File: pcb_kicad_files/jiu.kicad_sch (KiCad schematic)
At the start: 175 parts, among them J1 2x3 2.54mm pitch pin header, J2 TYPE-C-31-M-12, J3 1x5 2.54mm pitch pin header, J4 2x9 2.54mm pitch pin header, J5 Conn_01x02, Q1 2N7002, SW1 1U, SW10 1U, SW11 1U, SW12 1U, SW13 1U, SW14 1U, SW15 1U, SW16 2u, SW17 1.5U, SW18 1U, SW19 1U, SW2 1U, SW20 1U, SW21 1U, SW22 1U, SW23 1U, SW24 1U, SW25 1U, SW26 1U, SW27 1U, SW28 1U, SW29 1U, SW3 1U, SW30 1.5U, SW31 1U, SW32 1.75U, SW33 1U, SW34 1U, SW35 1U, SW36 1U, SW37 1U, SW38 1U, SW39 1U, SW4 1U, SW40 1U, SW41 1U, SW42 1U, SW43 1U, SW44 2.25U, SW45 1U, SW46 1.25U, SW47 2.25U, SW48 1U, SW49 1U, SW5 1U, SW50 1U, SW51 1U, SW52 1U, SW53 1U, SW54 1U, SW55 1U, SW56 1U, SW57 1U, SW58 1.75U, SW59 1U, SW6 1U, SW60 1U, SW61 1.5U, SW62 1U, SW63 1.5U, SW64 7U, SW65 1.5U, SW66 1U, SW67 1U, SW68 1U, SW69 1.25U, SW7 1U, SW70 1.25U, SW71 1.25U, SW72 6.25U, SW73 1.25U, SW8 1U, SW9 1U, U1 SRV05-4-P-T7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

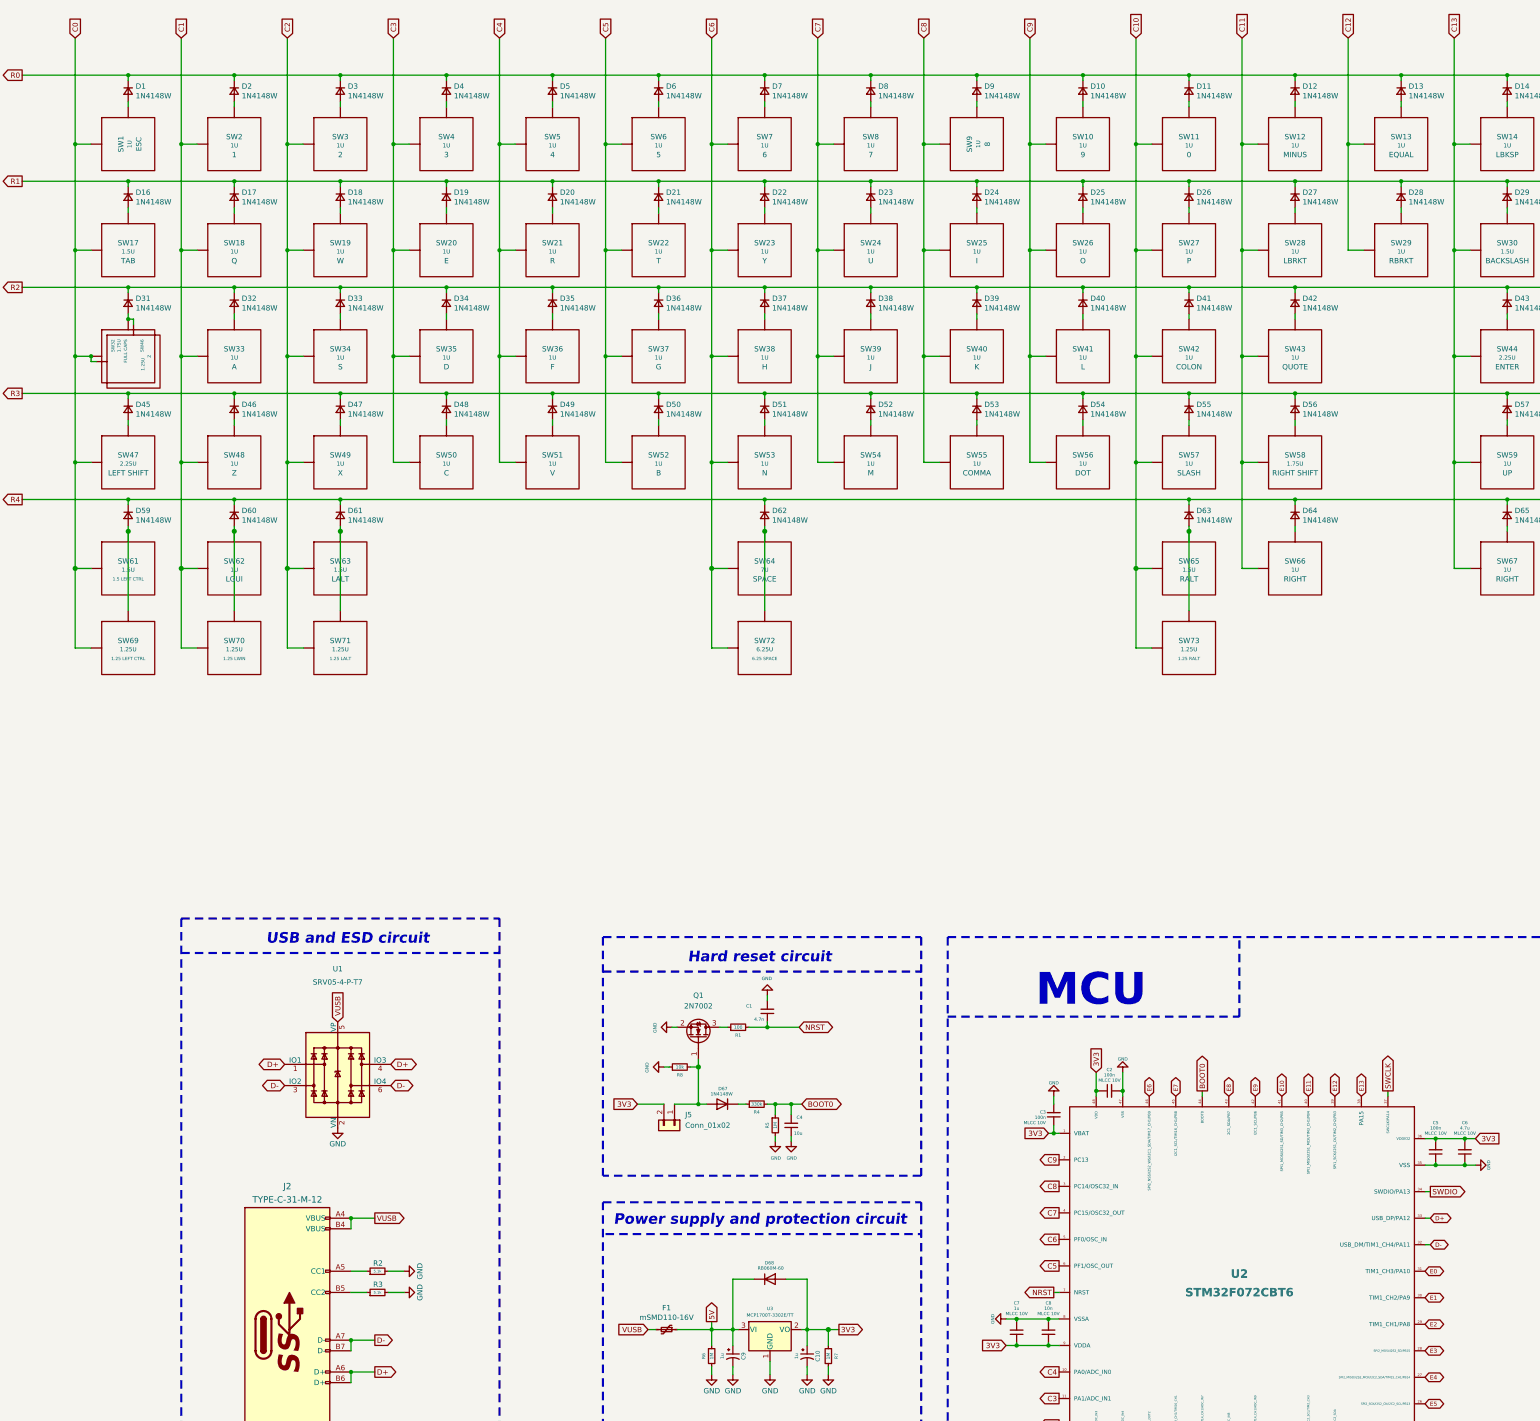
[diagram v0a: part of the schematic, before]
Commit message: Remove pin header connectors from BoM
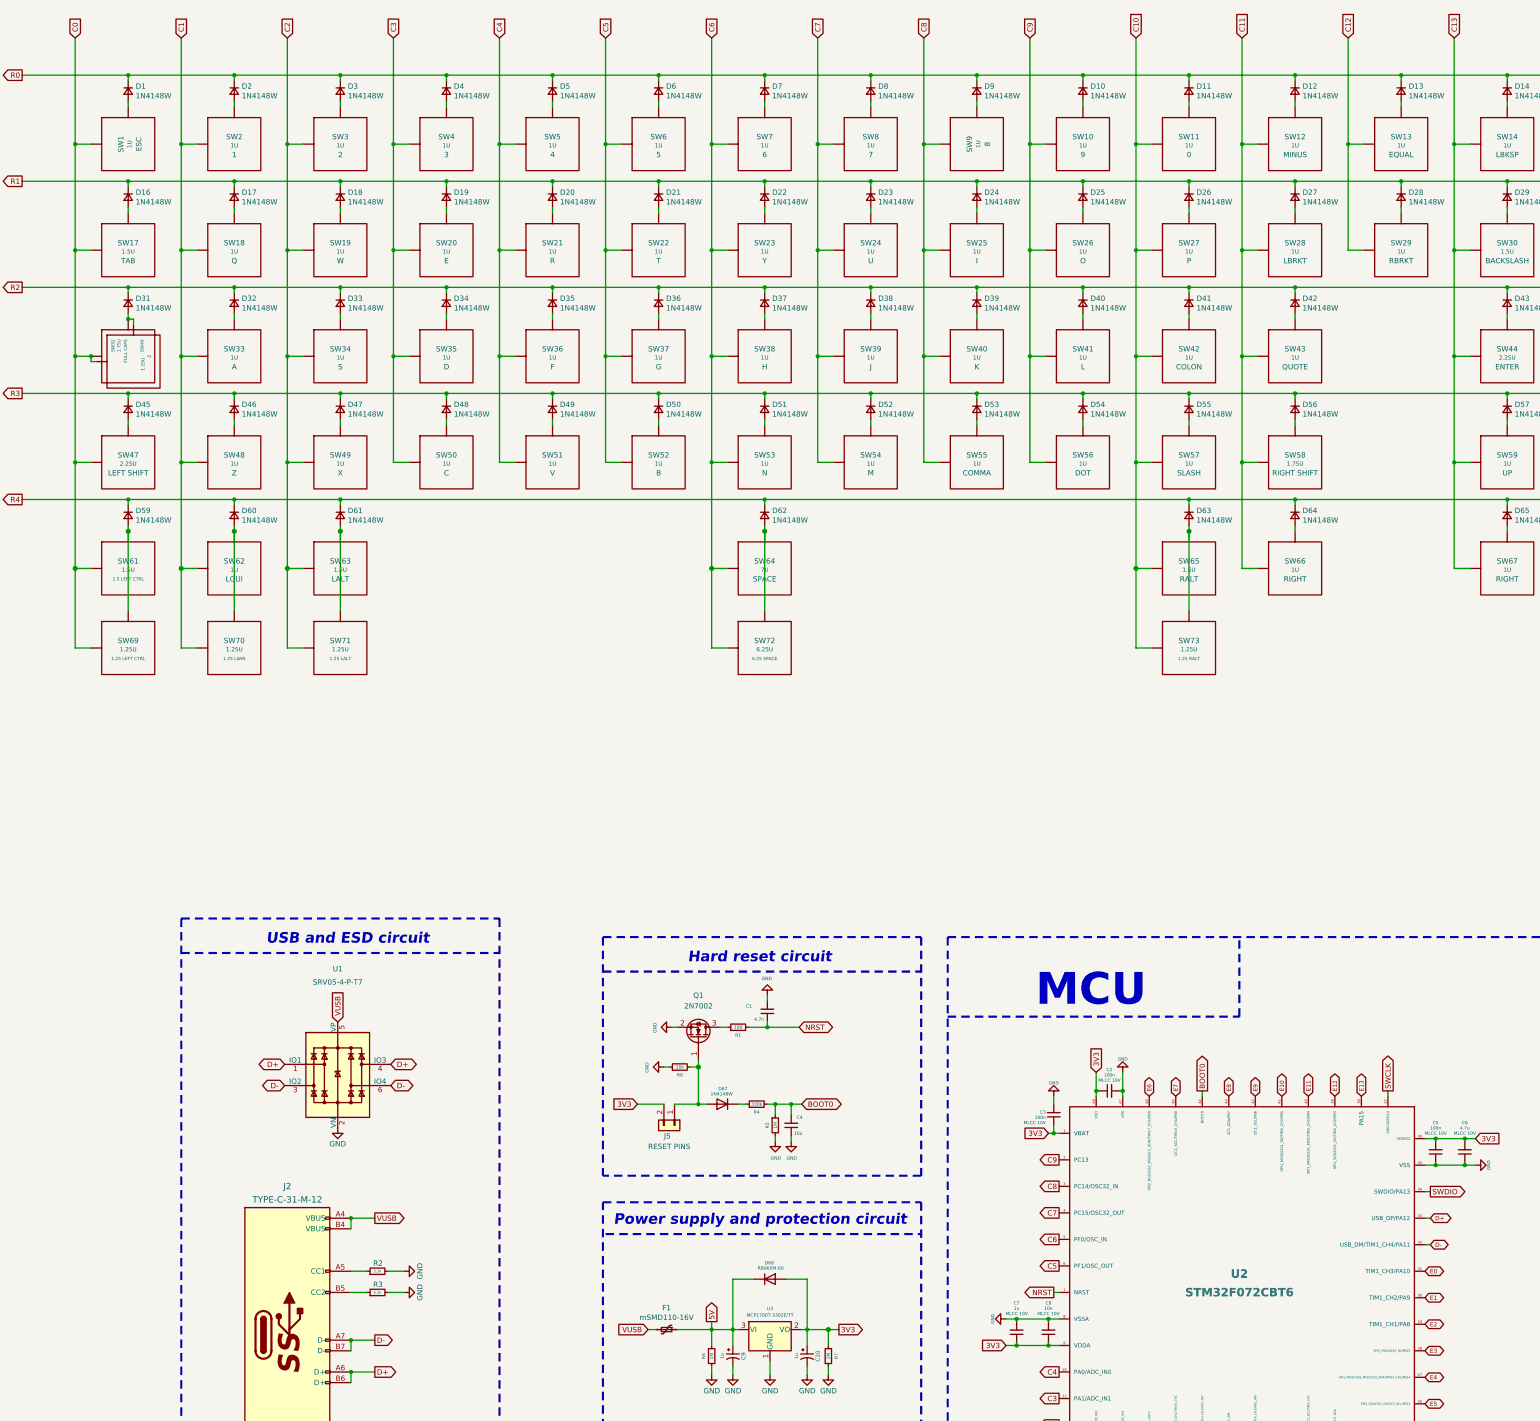
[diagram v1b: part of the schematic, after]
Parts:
- J3, J4: now left out of the parts list
- J5: value Conn_01x02 -> RESET PINS; Specification (none) -> Two THT pins for MCU hardware reset; now left out of the parts list
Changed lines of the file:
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@@
     (stroke (width 0) (type solid) (color 0 0 0 0))
   )
-  (wire (pts (xy 38.1 50.8) (xy 38.1 76.2))
+  (wire (pts (xy 38.1 50.8) (xy 41.91 50.8))
     (stroke (width 0) (type solid) (color 0 0 0 0))
   )
-  (wire (pts (xy 38.1 50.8) (xy 41.91 50.8))
+  (wire (pts (xy 38.1 76.2) (xy 38.1 50.8))
     (stroke (width 0) (type solid) (color 0 0 0 0))
   )
-  (wire (pts (xy 38.1 76.2) (xy 38.1 101.6))
+  (wire (pts (xy 38.1 101.6) (xy 38.1 76.2))
     (stroke (width 0) (type solid) (color 0 0 0 0))
   )
@@
     (stroke (width 0) (type solid) (color 0 0 0 0))
   )
-  (wire (pts (xy 50.8 110.49) (xy 76.2 110.49))
-    (stroke (width 0) (type solid) (color 0 0 0 0))
-  )
   (wire (pts (xy 50.8 111.76) (xy 50.8 110.49))
     (stroke (width 0) (type solid) (color 0 0 0 0))
@@
     (stroke (width 0) (type solid) (color 0 0 0 0))
   )
-  (wire (pts (xy 50.8 135.89) (xy 76.2 135.89))
-    (stroke (width 0) (type solid) (color 0 0 0 0))
-  )
   (wire (pts (xy 50.8 137.16) (xy 50.8 135.89))
     (stroke (width 0) (type solid) (color 0 0 0 0))
@@
     (stroke (width 0) (type solid) (color 0 0 0 0))
   )
-  (wire (pts (xy 76.2 59.69) (xy 101.6 59.69))
-    (stroke (width 0) (type solid) (color 0 0 0 0))
-  )
   (wire (pts (xy 76.2 66.04) (xy 76.2 67.31))
     (stroke (width 0) (type solid) (color 0 0 0 0))
@@
     (stroke (width 0) (type solid) (color 0 0 0 0))
   )
+  (wire (pts (xy 76.2 110.49) (xy 50.8 110.49))
+    (stroke (width 0) (type solid) (color 0 0 0 0))
+  )
   (wire (pts (xy 76.2 110.49) (xy 76.2 111.76))
     (stroke (width 0) (type solid) (color 0 0 0 0))
@@
     (stroke (width 0) (type solid) (color 0 0 0 0))
   )
+  (wire (pts (xy 76.2 135.89) (xy 50.8 135.89))
+    (stroke (width 0) (type solid) (color 0 0 0 0))
+  )
   (wire (pts (xy 76.2 135.89) (xy 76.2 137.16))
     (stroke (width 0) (type solid) (color 0 0 0 0))
@@
     (stroke (width 0) (type solid) (color 0 0 0 0))
   )
+  (wire (pts (xy 101.6 59.69) (xy 76.2 59.69))
+    (stroke (width 0) (type solid) (color 0 0 0 0))
+  )
   (wire (pts (xy 101.6 59.69) (xy 101.6 60.96))
     (stroke (width 0) (type solid) (color 0 0 0 0))
@@
     (stroke (width 0) (type solid) (color 0 0 0 0))
   )
-  (wire (pts (xy 177.8 85.09) (xy 203.2 85.09))
-    (stroke (width 0) (type solid) (color 0 0 0 0))
-  )
   (wire (pts (xy 177.8 91.44) (xy 177.8 92.71))
     (stroke (width 0) (type solid) (color 0 0 0 0))
@@
     (stroke (width 0) (type solid) (color 0 0 0 0))
   )
-  (wire (pts (xy 190.5 76.2) (xy 190.5 101.6))
+  (wire (pts (xy 190.5 101.6) (xy 190.5 76.2))
     (stroke (width 0) (type solid) (color 0 0 0 0))
   )
-  (wire (pts (xy 190.5 101.6) (xy 190.5 127))
+  (wire (pts (xy 190.5 127) (xy 190.5 101.6))
     (stroke (width 0) (type solid) (color 0 0 0 0))
   )
-  (wire (pts (xy 190.5 127) (xy 190.5 152.4))
+  (wire (pts (xy 190.5 152.4) (xy 190.5 127))
     (stroke (width 0) (type solid) (color 0 0 0 0))
   )
@@
     (stroke (width 0) (type solid) (color 0 0 0 0))
   )
-  (wire (pts (xy 190.5 334.645) (xy 195.58 334.645))
-    (stroke (width 0) (type solid) (color 0 0 0 0))
-  )
   (wire (pts (xy 190.5 343.535) (xy 190.5 345.44))
     (stroke (width 0) (type solid) (color 0 0 0 0))
@@
     (stroke (width 0) (type solid) (color 0 0 0 0))
   )
+  (wire (pts (xy 195.58 334.645) (xy 190.5 334.645))
+    (stroke (width 0) (type solid) (color 0 0 0 0))
+  )
   (wire (pts (xy 195.58 334.645) (xy 195.58 322.58))
     (stroke (width 0) (type solid) (color 0 0 0 0))
@@
     (stroke (width 0) (type solid) (color 0 0 0 0))
   )
+  (wire (pts (xy 203.2 85.09) (xy 177.8 85.09))
+    (stroke (width 0) (type solid) (color 0 0 0 0))
+  )
   (wire (pts (xy 203.2 85.09) (xy 203.2 86.36))
     (stroke (width 0) (type solid) (color 0 0 0 0))
@@
     (stroke (width 0) (type solid) (color 0 0 0 0))
   )
-  (wire (pts (xy 205.74 280.67) (xy 209.55 280.67))
-    (stroke (width 0) (type solid) (color 0 0 0 0))
-  )
   (wire (pts (xy 205.74 289.56) (xy 205.74 288.29))
     (stroke (width 0) (type solid) (color 0 0 0 0))
@@
     (stroke (width 0) (type solid) (color 0 0 0 0))
   )
+  (wire (pts (xy 209.55 280.67) (xy 205.74 280.67))
+    (stroke (width 0) (type solid) (color 0 0 0 0))
+  )
   (wire (pts (xy 209.55 280.67) (xy 209.55 283.21))
     (stroke (width 0) (type solid) (color 0 0 0 0))
@@
     (stroke (width 0) (type solid) (color 0 0 0 0))
   )
-  (wire (pts (xy 213.36 334.645) (xy 218.44 334.645))
-    (stroke (width 0) (type solid) (color 0 0 0 0))
-  )
   (wire (pts (xy 213.36 343.535) (xy 213.36 345.44))
     (stroke (width 0) (type solid) (color 0 0 0 0))
@@
     (stroke (width 0) (type solid) (color 0 0 0 0))
   )
+  (wire (pts (xy 218.44 334.645) (xy 213.36 334.645))
+    (stroke (width 0) (type solid) (color 0 0 0 0))
+  )
   (wire (pts (xy 218.44 334.645) (xy 218.44 338.455))
     (stroke (width 0) (type solid) (color 0 0 0 0))
@@
     (stroke (width 0) (type solid) (color 0 0 0 0))
   )
-  (wire (pts (xy 263.525 338.455) (xy 271.145 338.455))
-    (stroke (width 0) (type solid) (color 0 0 0 0))
-  )
   (wire (pts (xy 266.7 25.4) (xy 266.7 50.8))
     (stroke (width 0) (type solid) (color 0 0 0 0))
@@
     (stroke (width 0) (type solid) (color 0 0 0 0))
   )
+  (wire (pts (xy 271.145 338.455) (xy 263.525 338.455))
+    (stroke (width 0) (type solid) (color 0 0 0 0))
+  )
   (wire (pts (xy 271.145 338.455) (xy 273.685 338.455))
     (stroke (width 0) (type solid) (color 0 0 0 0))
@@
     (stroke (width 0) (type solid) (color 0 0 0 0))
   )
-  (wire (pts (xy 279.4 59.69) (xy 304.8 59.69))
-    (stroke (width 0) (type solid) (color 0 0 0 0))
-  )
   (wire (pts (xy 279.4 66.04) (xy 279.4 67.31))
     (stroke (width 0) (type solid) (color 0 0 0 0))
@@
     (stroke (width 0) (type solid) (color 0 0 0 0))
   )
-  (wire (pts (xy 304.8 34.29) (xy 330.2 34.29))
+  (wire (pts (xy 304.8 40.64) (xy 304.8 41.91))
     (stroke (width 0) (type solid) (color 0 0 0 0))
   )
-  (wire (pts (xy 304.8 40.64) (xy 304.8 41.91))
+  (wire (pts (xy 304.8 59.69) (xy 279.4 59.69))
     (stroke (width 0) (type solid) (color 0 0 0 0))
   )
@@
     (stroke (width 0) (type solid) (color 0 0 0 0))
   )
-  (wire (pts (xy 317.5 101.6) (xy 317.5 127))
+  (wire (pts (xy 317.5 127) (xy 317.5 101.6))
     (stroke (width 0) (type solid) (color 0 0 0 0))
   )
@@
     (stroke (width 0) (type solid) (color 0 0 0 0))
   )
+  (wire (pts (xy 330.2 34.29) (xy 304.8 34.29))
+    (stroke (width 0) (type solid) (color 0 0 0 0))
+  )
   (wire (pts (xy 330.2 34.29) (xy 330.2 35.56))
     (stroke (width 0) (type solid) (color 0 0 0 0))
@@
     (stroke (width 0) (type solid) (color 0 0 0 0))
   )
-  (wire (pts (xy 363.855 295.275) (xy 370.84 295.275))
-    (stroke (width 0) (type solid) (color 0 0 0 0))
-  )
   (wire (pts (xy 368.3 25.4) (xy 368.3 50.8))
     (stroke (width 0) (type solid) (color 0 0 0 0))
@@
     (stroke (width 0) (type solid) (color 0 0 0 0))
   )
+  (wire (pts (xy 370.84 295.275) (xy 363.855 295.275))
+    (stroke (width 0) (type solid) (color 0 0 0 0))
+  )
   (wire (pts (xy 370.84 295.275) (xy 373.38 295.275))
     (stroke (width 0) (type solid) (color 0 0 0 0))
@@
   )
   (symbol (lib_id "Connector_Generic:Conn_01x02") (at 181.61 285.75 270) (unit 1)
-    (in_bom yes) (on_board yes)
-    (property "Reference" "J5" (id 0) (at 184.15 283.21 90)
-      (effects (font (size 1.27 1.27)) (justify left))
-    )
-    (property "Value" "Conn_01x02" (id 1) (at 184.15 285.75 90)
+    (in_bom no) (on_board yes)
+    (property "Reference" "J5" (id 0) (at 179.07 288.29 90)
       (effects (font (size 1.27 1.27)) (justify left))
     )
+    (property "Value" "RESET PINS" (id 1) (at 180.34 290.83 90))
     (property "Footprint" "acheron_Hardware:THT_reset_contacts" (id 2) (at 181.61 285.75 0)
       (effects (font (size 1.27 1.27)) hide)
@@
       (effects (font (size 1.27 1.27)) hide)
     )
+    (property "Specification" "Two THT pins for MCU hardware reset" (id 4) (at 181.61 285.75 0)
+      (effects (font (size 1.27 1.27)) hide)
+    )
     (pin "1")
     (pin "2")
@@
   )
   (symbol (lib_id "Connector_Generic:Conn_01x05") (at 407.035 314.96 0) (unit 1)
-    (in_bom yes) (on_board yes)
+    (in_bom no) (on_board yes)
     (property "Reference" "J3" (id 0) (at 407.035 303.7586 0))
     (property "Value" "1x5 2.54mm pitch pin header" (id 1) (at 407.035 306.07 0))
@@
   )
   (symbol (lib_id "Connector_Generic:Conn_02x09_Odd_Even") (at 416.56 350.52 0) (unit 1)
-    (in_bom yes) (on_board yes)
+    (in_bom no) (on_board yes)
     (property "Reference" "J4" (id 0) (at 416.56 334.2386 0))
     (property "Value" "2x9 2.54mm pitch pin header" (id 1) (at 416.56 336.55 0))
@@
     )
     (path "/aaf15ef2-4849-448a-b156-9ea8d20ecfb4"
-      (reference "J5") (unit 1) (value "Conn_01x02") (footprint "acheron_Hardware:THT_reset_contacts")
+      (reference "J5") (unit 1) (value "RESET PINS") (footprint "acheron_Hardware:THT_reset_contacts")
     )
     (path "/51170fe8-c56e-430a-bd4e-d0d55312b20b"

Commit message: Pin row 4 to B13, change extra pin header to 2x8 from 2x9
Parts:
- J4: footprint acheron_Connectors:PinHeader_2x9_P2.54mm_Vertical -> acheron_Connectors:PinHeader_2x8_P2.54mm_Vertical; symbol Connector_Generic:Conn_02x09_Odd_Even -> Connector_Generic:Conn_02x08_Odd_Even; now in the parts list
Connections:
- net 3V3: now also J4.3 (Pin_3); no longer J4.5 (Pin_5)
- net 5V: now also J4.1 (Pin_1); no longer J4.3 (Pin_3)
- net E0: now also J4.5 (Pin_5); no longer J4.7 (Pin_7)
- net E1: now also J4.7 (Pin_7); no longer J4.9 (Pin_9)
- net E10: now also J4.8 (Pin_8); no longer J4.10 (Pin_10)
- net E11: now also J4.6 (Pin_6); no longer J4.8 (Pin_8)
- net E12: now also J4.4 (Pin_4); no longer J4.6 (Pin_6)
- net E13: now also J4.2 (Pin_2); no longer J4.4 (Pin_4)
- net E2: now also J4.9 (Pin_9); no longer J4.11 (Pin_11)
- net E3: now also J4.11 (Pin_11); no longer J4.13 (Pin_13)
- net E4: now also J4.13 (Pin_13); no longer J4.15 (Pin_15)
- net E6: now also J4.16 (Pin_16); no longer J4.18 (Pin_18)
- net E7: now also J4.14 (Pin_14); no longer J4.16 (Pin_16)
- net E8: now also J4.12 (Pin_12); no longer J4.14 (Pin_14)
- net E9: now also J4.10 (Pin_10); no longer J4.12 (Pin_12)
- net GND: now also J4.15 (Pin_15); no longer J4.1 (Pin_1), J4.2 (Pin_2)
- net R4: now also U2.26 (SPI2_SCK/I2S2_CK/I2C2_SCL/PB13)
- removed net E5: J4.17 (Pin_17), U2.26 (SPI2_SCK/I2S2_CK/I2C2_SCL/PB13)
